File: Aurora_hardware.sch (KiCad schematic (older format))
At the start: 56 parts, among them J1 DIGITALOUTNI, J2 INRELAY, U1 4081, U2 4081, U3 4081, U4 4081, U5 4081

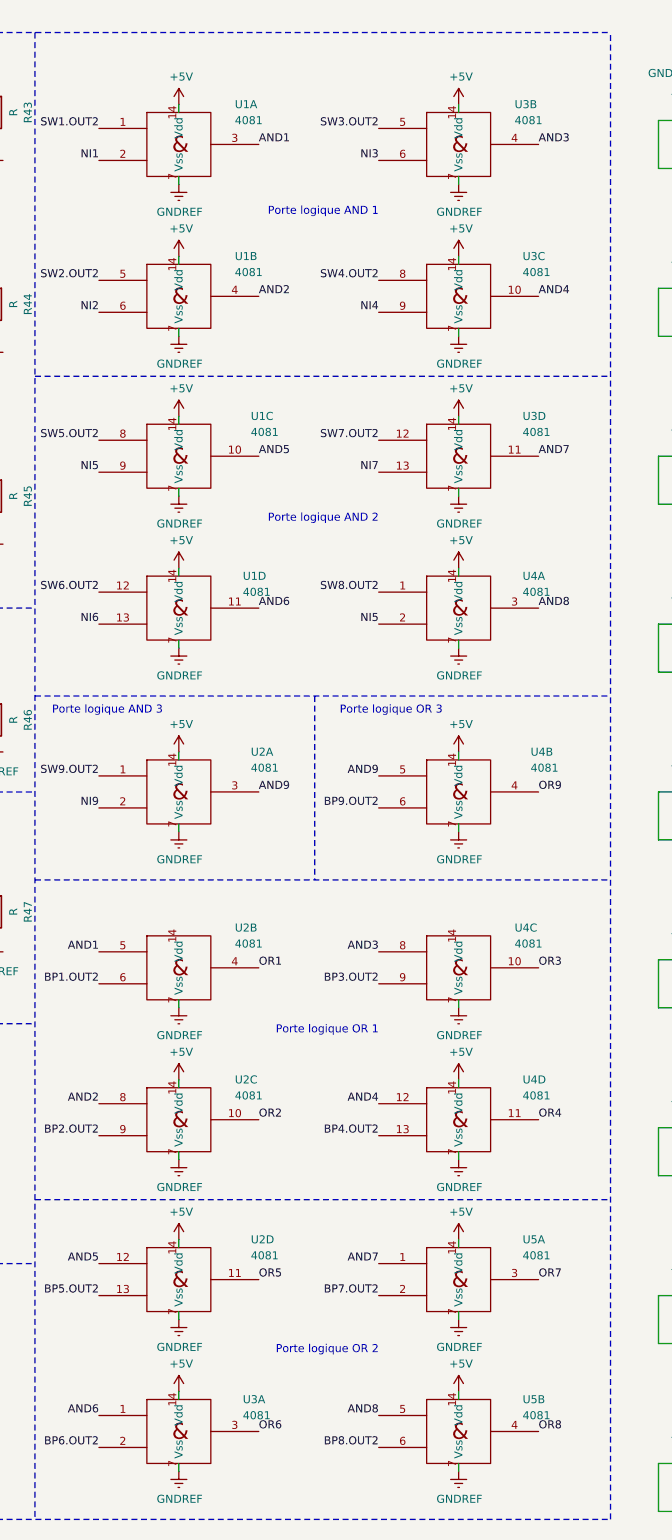
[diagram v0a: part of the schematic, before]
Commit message: pose des empreintes sur les composants
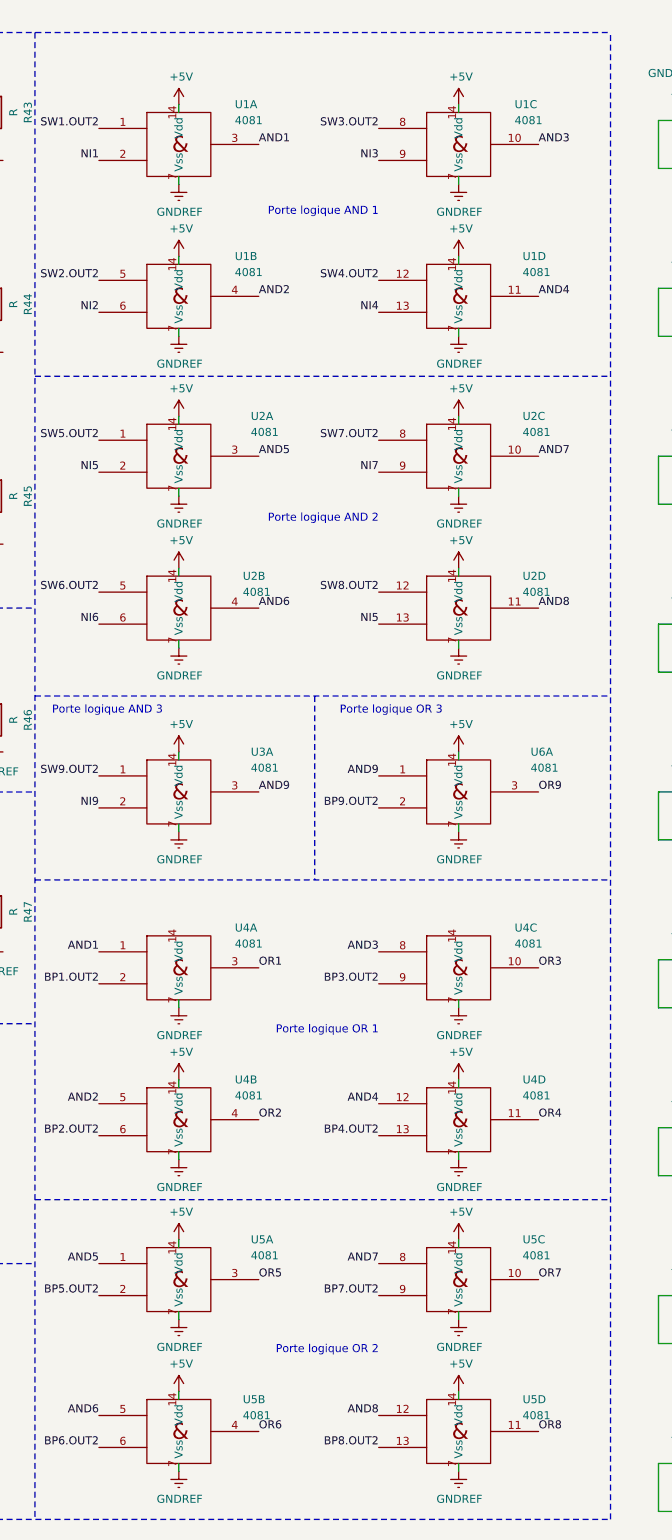
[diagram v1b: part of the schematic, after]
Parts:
- J1: footprint (none) -> Connector_PinHeader_1.27mm:PinHeader_1x10_P1.27mm_Vertical
- J2: footprint (none) -> Connector_PinHeader_1.27mm:PinHeader_1x11_P1.27mm_Vertical
- JPP1, JPP2: footprint (none) -> Connector_Dsub:DSUB-62-HD_Female_Horizontal_P2.41x1.98mm_EdgePinOffset9.40mm
- R1, R10, R11, R12, R13, R14, R15, R16, R17, R18, R19, R2, R20, R21, R22, R23, R24, R25, R26, R27, R28, R29, R3, R30, R31, R32, R33, R34, R35, R36, R37, R38, R39, R4, R40, R41, R42, R43, R44, R45, R46, R47, R5, R6, R7, R8, R9: footprint (none) -> Resistor_THT:R_Axial_DIN0204_L3.6mm_D1.6mm_P7.62mm_Horizontal
- U1, U4, U5: footprint (none) -> Package_DIP:DIP-14_W7.62mm
- U1, U2, U5: renamed from U3; footprint (none) -> Package_DIP:DIP-14_W7.62mm
- U2: renamed from U1; footprint (none) -> Package_DIP:DIP-14_W7.62mm
- U2, U6: renamed from U4; footprint (none) -> Package_DIP:DIP-14_W7.62mm
- U3, U4, U5: renamed from U2; footprint (none) -> Package_DIP:DIP-14_W7.62mm
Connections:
- net AND1: now also U4.1; no longer U4.5
- net AND2: now also U4.5; no longer U4.8
- net AND3: now also U1.10; no longer U1.4
- net AND4: now also U1.11; no longer U1.10
- net AND5: now also U2.3, U5.1; no longer U2.10, U5.12
- net AND6: now also U2.4, U5.5; no longer U2.11, U5.1
- net AND7: now also U2.10, U5.8; no longer U2.11, U5.1
- net AND8: now also U2.11, U5.12; no longer U2.3, U5.5
- net AND9: now also U6.1; no longer U6.5
- net BP1.OUT2: now also U4.2; no longer U4.6
- net BP2.OUT2: now also U4.6; no longer U4.9
- net BP5.OUT2: now also U5.2; no longer U5.13
- net BP6.OUT2: now also U5.6; no longer U5.2
- net BP7.OUT2: now also U5.9; no longer U5.2
- net BP8.OUT2: now also U5.13; no longer U5.6
- net BP9.OUT2: now also U6.2; no longer U6.6
- net NI3: now also U1.9; no longer U1.6
- net NI4: now also U1.13; no longer U1.9
- net NI5: now also U2.13, U2.2; no longer U2.2, U2.9
- net NI6: now also U2.6; no longer U2.13
- net NI7: now also U2.9; no longer U2.13
- net OR1: now also U4.3; no longer U4.4
- net OR2: now also U4.4; no longer U4.10
- net OR5: now also U5.3; no longer U5.11
- net OR6: now also U5.4; no longer U5.3
- net OR7: now also U5.10; no longer U5.3
- net OR8: now also U5.11; no longer U5.4
- net OR9: now also U6.3; no longer U6.4
- net SW3.OUT2: now also U1.8; no longer U1.5
- net SW4.OUT2: now also U1.12; no longer U1.8
- net SW5.OUT2: now also U2.1; no longer U2.8
- net SW6.OUT2: now also U2.5; no longer U2.12
- net SW7.OUT2: now also U2.8; no longer U2.12
- net SW8.OUT2: now also U2.12; no longer U2.1

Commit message: Add ALIM PLUGS
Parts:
- added J3, J4: Conn_01x02_Female, Connector:Banana_Jack_2Pin, symbol Connector:Conn_01x02_Female
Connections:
- net +24V: now also J4.1 (Pin_1)
- net +5V: now also J3.1 (Pin_1)
- net GND: now also J4.2 (Pin_2)
- net GNDREF: now also J3.2 (Pin_2)
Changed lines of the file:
@@
 	-1   0    0    1
 $EndComp
-Wire Wire Line
-	9250 1100 9300 1100
 $Comp
 L Connector:DSub_62pinMale JPP1
@@
 	1    0    0    -1
 $EndComp
-$Comp
-L power:+5V #PWR0101
-U 1 1 5F640402
-P 9250 1100
-F 0 "#PWR0101" H 9250 950 50  0001 C CNN
-F 1 "+5V" H 9265 1273 50  0000 C CNN
-F 2 "" H 9250 1100 50  0001 C CNN
-F 3 "" H 9250 1100 50  0001 C CNN
-	1    9250 1100
-	1    0    0    -1
-$EndComp
-$Comp
-L power:GNDREF #PWR0102
-U 1 1 5F656F3C
-P 9200 1250
-F 0 "#PWR0102" H 9200 1000 50  0001 C CNN
-F 1 "GNDREF" V 9205 1122 50  0000 R CNN
-F 2 "" H 9200 1250 50  0001 C CNN
-F 3 "" H 9200 1250 50  0001 C CNN
-	1    9200 1250
-	0    1    1    0
-$EndComp
-Wire Wire Line
-	9200 1250 9300 1250
 $Comp
 L power:+5V #PWR0103
@@
 Wire Notes Line
 	1350 8700 4950 8700
+$Comp
+L Connector:Conn_01x02_Female J3
+U 1 1 5F11A5B0
+P 4000 7500
+F 0 "J3" H 4028 7476 50  0000 L CNN
+F 1 "Conn_01x02_Female" H 4028 7385 50  0000 L CNN
+F 2 "Connector:Banana_Jack_2Pin" H 4000 7500 50  0001 C CNN
+F 3 "~" H 4000 7500 50  0001 C CNN
+	1    4000 7500
+	1    0    0    -1
+$EndComp
+$Comp
+L Connector:Conn_01x02_Female J4
+U 1 1 5F11CE09
+P 4000 8200
+F 0 "J4" H 4028 8176 50  0000 L CNN
+F 1 "Conn_01x02_Female" H 4028 8085 50  0000 L CNN
+F 2 "Connector:Banana_Jack_2Pin" H 4000 8200 50  0001 C CNN
+F 3 "~" H 4000 8200 50  0001 C CNN
+	1    4000 8200
+	1    0    0    -1
+$EndComp
 Wire Notes Line
-	3150 8700 3150 10300
+	3150 7200 3150 10300
+$Comp
+L power:+5V #PWR0153
+U 1 1 5F12615D
+P 3750 7450
+F 0 "#PWR0153" H 3750 7300 50  0001 C CNN
+F 1 "+5V" H 3765 7623 50  0000 C CNN
+F 2 "" H 3750 7450 50  0001 C CNN
+F 3 "" H 3750 7450 50  0001 C CNN
+	1    3750 7450
+	1    0    0    -1
+$EndComp
+$Comp
+L power:GND #PWR0154
+U 1 1 5F1282AD
+P 3750 8350
+F 0 "#PWR0154" H 3750 8100 50  0001 C CNN
+F 1 "GND" H 3755 8177 50  0000 C CNN
+F 2 "" H 3750 8350 50  0001 C CNN
+F 3 "" H 3750 8350 50  0001 C CNN
+	1    3750 8350
+	1    0    0    -1
+$EndComp
+$Comp
+L power:+24V #PWR0155
+U 1 1 5F129628
+P 3750 8150
+F 0 "#PWR0155" H 3750 8000 50  0001 C CNN
+F 1 "+24V" H 3765 8323 50  0000 C CNN
+F 2 "" H 3750 8150 50  0001 C CNN
+F 3 "" H 3750 8150 50  0001 C CNN
+	1    3750 8150
+	1    0    0    -1
+$EndComp
+$Comp
+L power:GNDREF #PWR0156
+U 1 1 5F12AA85
+P 3750 7650
+F 0 "#PWR0156" H 3750 7400 50  0001 C CNN
+F 1 "GNDREF" H 3755 7477 50  0000 C CNN
+F 2 "" H 3750 7650 50  0001 C CNN
+F 3 "" H 3750 7650 50  0001 C CNN
+	1    3750 7650
+	1    0    0    -1
+$EndComp
+Wire Wire Line
+	3800 7500 3750 7500
+Wire Wire Line
+	3750 7500 3750 7450
+Wire Wire Line
+	3800 7600 3750 7600
+Wire Wire Line
+	3750 7600 3750 7650
+Wire Wire Line
+	3750 8150 3750 8200
+Wire Wire Line
+	3750 8200 3800 8200
+Wire Wire Line
+	3800 8300 3750 8300
+Wire Wire Line
+	3750 8300 3750 8350
+$Comp
+L power:GNDREF #PWR0102
+U 1 1 5F656F3C
+P 9200 1250
+F 0 "#PWR0102" H 9200 1000 50  0001 C CNN
+F 1 "GNDREF" V 9205 1122 50  0000 R CNN
+F 2 "" H 9200 1250 50  0001 C CNN
+F 3 "" H 9200 1250 50  0001 C CNN
+	1    9200 1250
+	0    1    1    0
+$EndComp
+Wire Wire Line
+	9200 1250 9300 1250
+Wire Wire Line
+	9250 1100 9300 1100
+$Comp
+L power:+5V #PWR0101
+U 1 1 5F640402
+P 9250 1100
+F 0 "#PWR0101" H 9250 950 50  0001 C CNN
+F 1 "+5V" H 9265 1273 50  0000 C CNN
+F 2 "" H 9250 1100 50  0001 C CNN
+F 3 "" H 9250 1100 50  0001 C CNN
+	1    9250 1100
+	1    0    0    -1
+$EndComp
 $EndSCHEMATC
